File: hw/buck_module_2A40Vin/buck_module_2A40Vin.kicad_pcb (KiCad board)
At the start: 2 copper layers, 40 x 24 mm, 22 parts, among them IC1 LV14240DDAR, J1 Conn_01x06, J2 Conn_01x06

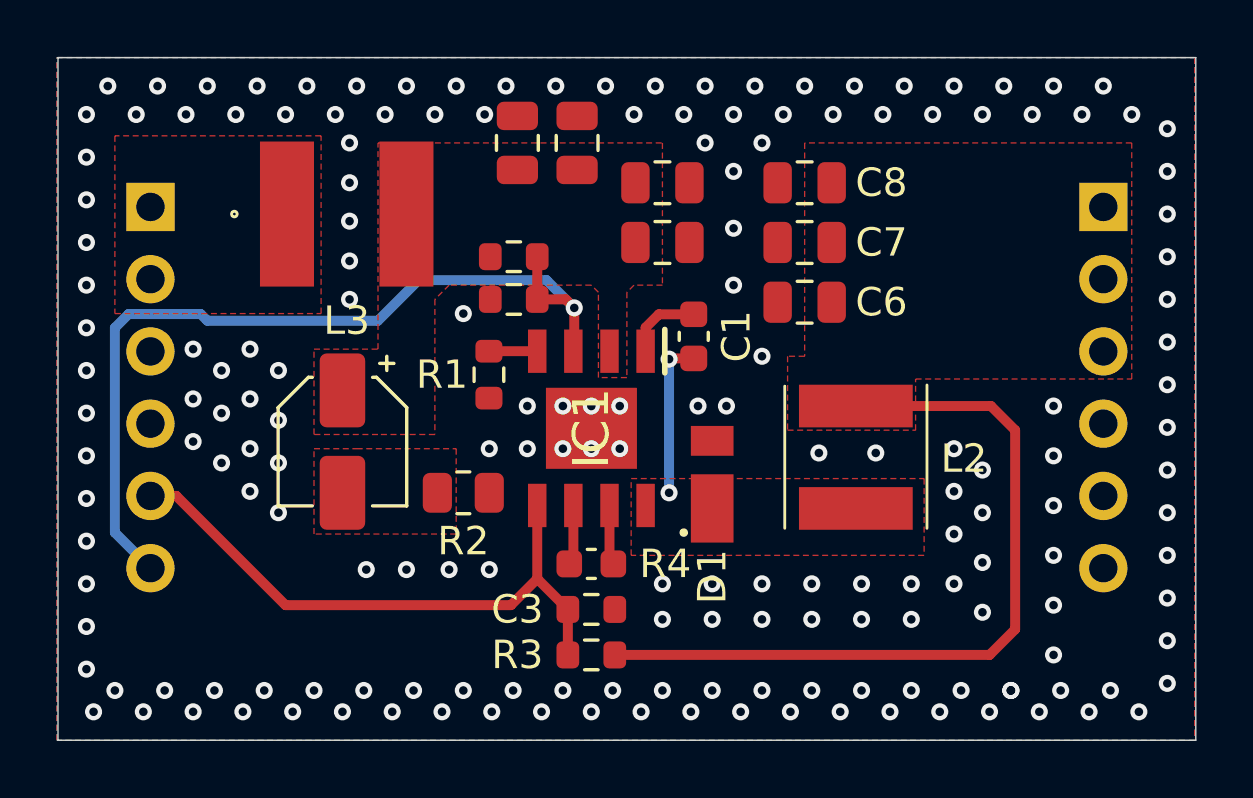
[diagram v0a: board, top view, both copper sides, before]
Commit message: Added silkscreen markings on the PCB
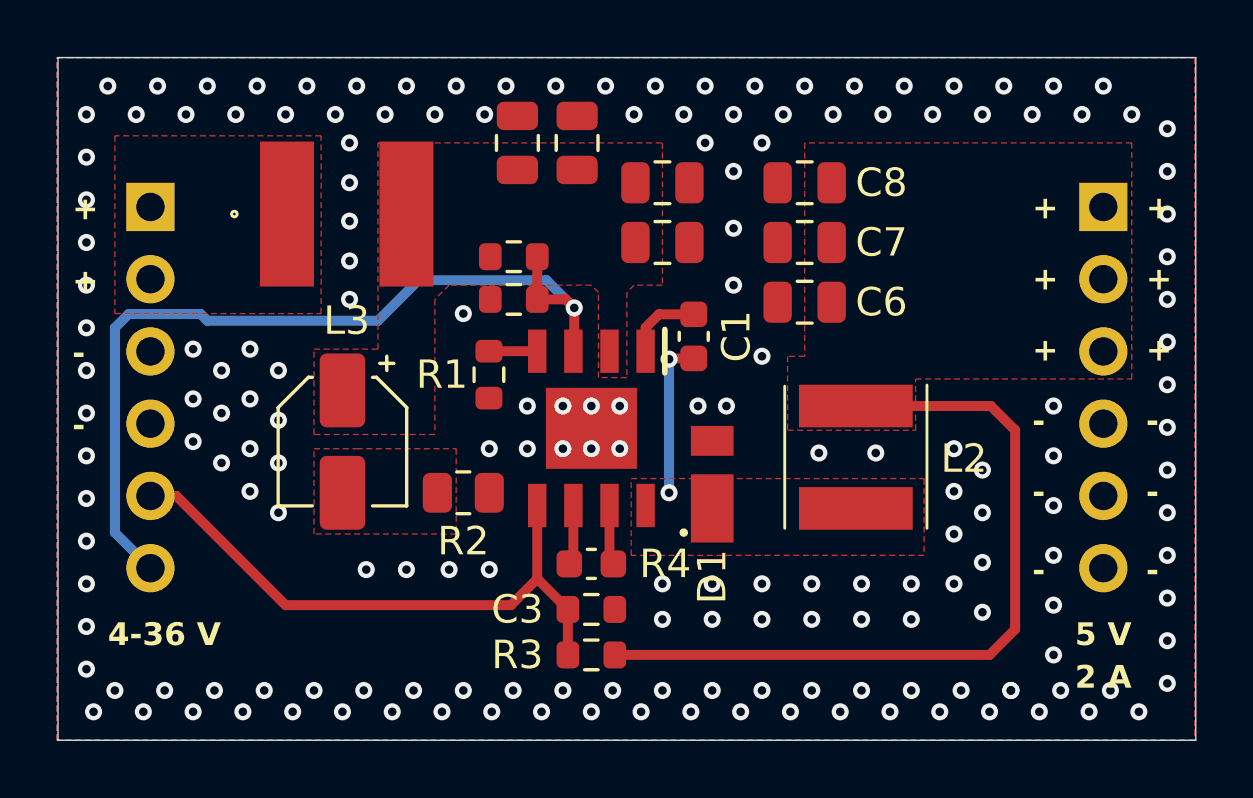
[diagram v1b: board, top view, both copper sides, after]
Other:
- board text added: "+"
- board text added: "-"
- board text added: "2 A"
- board text added: "4-36 V"
- board text added: "5 V"
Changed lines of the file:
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@@
 		(tags "Integrated Circuit")
 		(property "Reference" "IC1"
-			(at 0 0 90)
+			(at 0 0 0)
 			(layer "F.SilkS")
+			(hide yes)
 			(effects
 				(font
-					(size 1.27 1.27)
-					(thickness 0.254)
+					(size 1 1)
+					(thickness 0.15)
 				)
 			)
@@
 		(layer "Edge.Cuts")
 	)
+	(gr_text "5 V"
+		(at 132 102.75 0)
+		(layer "F.SilkS")
+		(effects
+			(font
+				(size 0.8 0.8)
+				(thickness 0.16)
+				(bold yes)
+			)
+			(justify left bottom)
+		)
+	)
+	(gr_text "+"
+		(at 134.5 90.25 0)
+		(layer "F.SilkS")
+		(effects
+			(font
+				(size 0.8 0.8)
+				(thickness 0.16)
+				(bold yes)
+			)
+			(justify left bottom)
+		)
+	)
+	(gr_text "+"
+		(at 130.5 90.25 0)
+		(layer "F.SilkS")
+		(effects
+			(font
+				(size 0.8 0.8)
+				(thickness 0.16)
+				(bold yes)
+			)
+			(justify left bottom)
+		)
+	)
+	(gr_text "-"
+		(at 134.5 95.25 0)
+		(layer "F.SilkS")
+		(effects
+			(font
+				(size 0.8 0.8)
+				(thickness 0.16)
+				(bold yes)
+			)
+			(justify left bottom)
+		)
+	)
+	(gr_text "-"
+		(at 130.5 100.5 0)
+		(layer "F.SilkS")
+		(effects
+			(font
+				(size 0.8 0.8)
+				(thickness 0.16)
+				(bold yes)
+			)
+			(justify left bottom)
+		)
+	)
+	(gr_text "-"
+		(at 134.5 97.75 0)
+		(layer "F.SilkS")
+		(effects
+			(font
+				(size 0.8 0.8)
+				(thickness 0.16)
+				(bold yes)
+			)
+			(justify left bottom)
+		)
+	)
+	(gr_text "+"
+		(at 130.5 87.75 0)
+		(layer "F.SilkS")
+		(effects
+			(font
+				(size 0.8 0.8)
+				(thickness 0.16)
+				(bold yes)
+			)
+			(justify left bottom)
+		)
+	)
+	(gr_text "-"
+		(at 96.75 95.4012 0)
+		(layer "F.SilkS")
+		(effects
+			(font
+				(size 0.8 0.8)
+				(thickness 0.16)
+				(bold yes)
+			)
+			(justify left bottom)
+		)
+	)
+	(gr_text "+"
+		(at 130.5 92.75 0)
+		(layer "F.SilkS")
+		(effects
+			(font
+				(size 0.8 0.8)
+				(thickness 0.16)
+				(bold yes)
+			)
+			(justify left bottom)
+		)
+	)
+	(gr_text "+"
+		(at 96.75 87.7812 0)
+		(layer "F.SilkS")
+		(effects
+			(font
+				(size 0.8 0.8)
+				(thickness 0.16)
+				(bold yes)
+			)
+			(justify left bottom)
+		)
+	)
+	(gr_text "+"
+		(at 96.75 90.3212 0)
+		(layer "F.SilkS")
+		(effects
+			(font
+				(size 0.8 0.8)
+				(thickness 0.16)
+				(bold yes)
+			)
+			(justify left bottom)
+		)
+	)
+	(gr_text "+"
+		(at 134.5 87.75 0)
+		(layer "F.SilkS")
+		(effects
+			(font
+				(size 0.8 0.8)
+				(thickness 0.16)
+				(bold yes)
+			)
+			(justify left bottom)
+		)
+	)
+	(gr_text "-"
+		(at 134.5 100.5 0)
+		(layer "F.SilkS")
+		(effects
+			(font
+				(size 0.8 0.8)
+				(thickness 0.16)
+				(bold yes)
+			)
+			(justify left bottom)
+		)
+	)
+	(gr_text "2 A"
+		(at 132 104.25 0)
+		(layer "F.SilkS")
+		(effects
+			(font
+				(size 0.8 0.8)
+				(thickness 0.16)
+				(bold yes)
+			)
+			(justify left bottom)
+		)
+	)
+	(gr_text "-"
+		(at 130.5 97.75 0)
+		(layer "F.SilkS")
+		(effects
+			(font
+				(size 0.8 0.8)
+				(thickness 0.16)
+				(bold yes)
+			)
+			(justify left bottom)
+		)
+	)
+	(gr_text "4-36 V"
+		(at 98 102.75 0)
+		(layer "F.SilkS")
+		(effects
+			(font
+				(size 0.8 0.8)
+				(thickness 0.16)
+				(bold yes)
+			)
+			(justify left bottom)
+		)
+	)
+	(gr_text "+"
+		(at 134.5 92.75 0)
+		(layer "F.SilkS")
+		(effects
+			(font
+				(size 0.8 0.8)
+				(thickness 0.16)
+				(bold yes)
+			)
+			(justify left bottom)
+		)
+	)
+	(gr_text "-"
+		(at 130.5 95.25 0)
+		(layer "F.SilkS")
+		(effects
+			(font
+				(size 0.8 0.8)
+				(thickness 0.16)
+				(bold yes)
+			)
+			(justify left bottom)
+		)
+	)
+	(gr_text "-"
+		(at 96.75 92.8612 0)
+		(layer "F.SilkS")
+		(effects
+			(font
+				(size 0.8 0.8)
+				(thickness 0.16)
+				(bold yes)
+			)
+			(justify left bottom)
+		)
+	)
 	(dimension
 		(type orthogonal)
@@
 	)
 	(zone
-		(net 9)
-		(net_name "/FB")
+		(net 11)
+		(net_name "/EN")
 		(layer "F.Cu")
 		(name "$teardrop_padvia$")
 		(hatch none 0.1)
-		(priority 30000)
+		(priority 30007)
 		(attr
 			(teardrop
@@
 		(polygon
 			(pts
-				(xy 100.840392 97.592905) (xy 100.608807 97.380513) (xy 100.573212 97.350725) (xy 100.40477 97.196781)
-				(xy 100.315078 97.090122) (xy 100.206749 96.937765) (xy 99.499293 97.409293) (xy 99.972235 98.116749)
-				(xy 100.105205 98.008791) (xy 100.195029 97.918501) (xy 100.291376 97.823731) (xy 100.337267 97.788525)
-				(xy 100.38327 97.764976) (xy 100.43061 97.755736) (xy 100.480512 97.763457) (xy 100.534202 97.790791)
-				(xy 100.592905 97.840392)
+				(xy 114.225 91.364537) (xy 114.225043 91.373968) (xy 114.222956 91.43058) (xy 114.206097 91.491301)
+				(xy 114.18747 91.518082) (xy 114.159559 91.539747) (xy 114.120501 91.554248) (xy 114.068433 91.559537)
+				(xy 114.368582 92.323037) (xy 114.693582 91.559537) (xy 114.65125 91.554828) (xy 114.619985 91.541862)
+				(xy 114.58474 91.499489) (xy 114.572886 91.432715) (xy 114.574075 91.389295) (xy 114.575 91.364537)
 			)
 		)
 	)
 	(zone
-		(net 11)
-		(net_name "/EN")
+		(net 9)
+		(net_name "/FB")
 		(layer "F.Cu")
 		(name "$teardrop_padvia$")
 		(hatch none 0.1)
-		(priority 30007)
+		(priority 30000)
 		(attr
 			(teardrop
@@
 		(polygon
 			(pts
-				(xy 114.225 91.364537) (xy 114.225043 91.373968) (xy 114.222956 91.43058) (xy 114.206097 91.491301)
-				(xy 114.18747 91.518082) (xy 114.159559 91.539747) (xy 114.120501 91.554248) (xy 114.068433 91.559537)
-				(xy 114.368582 92.323037) (xy 114.693582 91.559537) (xy 114.65125 91.554828) (xy 114.619985 91.541862)
-				(xy 114.58474 91.499489) (xy 114.572886 91.432715) (xy 114.574075 91.389295) (xy 114.575 91.364537)
+				(xy 100.840392 97.592905) (xy 100.608807 97.380513) (xy 100.573212 97.350725) (xy 100.40477 97.196781)
+				(xy 100.315078 97.090122) (xy 100.206749 96.937765) (xy 99.499293 97.409293) (xy 99.972235 98.116749)
+				(xy 100.105205 98.008791) (xy 100.195029 97.918501) (xy 100.291376 97.823731) (xy 100.337267 97.788525)
+				(xy 100.38327 97.764976) (xy 100.43061 97.755736) (xy 100.480512 97.763457) (xy 100.534202 97.790791)
+				(xy 100.592905 97.840392)
 			)
 		)
